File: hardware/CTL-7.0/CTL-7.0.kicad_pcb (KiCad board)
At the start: 2 copper layers, 18 parts, among them J2 Left, J3 Right, U1 STM32H750VBTx, U2 AMS1117-3.3, Y1 32.768K, Y2 25MHz

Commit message: modified:   Ferrite Transformer Calculation.xlsx 	modified:   archive/Peripheral Migration ESP32S3-STM32H7.md 	renamed:    archive/PR_ 0201_2026.docx -> archive/Purchase 20260201.docx 	new file:   archive/Purchase 20260720.docx 	new file:   archive/Purchase Plan/bom.csv 	new file:   archive/Purchase Plan/bom.xlsx 	new file:   archive/Purchase Recaps.xlsx 	modified:   archive/REM - Vsense.xlsx 	new file:   archive/datasheets/SPC7040.PDF 	new file:   archive/datasheets/rm0433-stm32h742-stm32h743-753-and-stm32h750-value-line-advanced-armbased-32bit-mcus-stmicroelectronics.pdf 	new file:   archive/refferences/MiniSTM32H7xx-master/.gitattributes 	new file:   archive/refferences/MiniSTM32H7xx-master/.gitignore 	new file:   archive/refferences/MiniSTM32H7xx-master/Datasheet/MCU/DM00287603_ZHV2.pdf 	new file:   "archive/refferences/MiniSTM32H7xx-master/Datasheet/MCU/ES0396_STM32H750xB\345\222\214STM32H753xI\345\215\225\347\211\207\346\234\272\347\232\204\345\261\200\351\231\220\346\200\247.pdf" 	new file:   "archive/refferences/MiniSTM32H7xx-master/Datasheet/MCU/PM0253_STM32F7\345\222\214 STM32H7\345\215\225\347\211\207\346\234\272\347\274\226\347\250\213\346\211\213\345\206\214.pdf" 	new file:   "archive/refferences/MiniSTM32H7xx-master/Datasheet/MCU/RM0433_STM32H7x3\345\222\214STM32H750\345\215\225\347\211\207\346\234\272\345\217\202\350\200\203\346\211\213\345\206\214.pdf" 	new file:   archive/refferences/MiniSTM32H7xx-master/Datasheet/MCU/STM32H743VI_Datasheet.pdf 	new file:   archive/refferences/MiniSTM32H7xx-master/Datasheet/MCU/STM32H750VB_Datasheet.pdf 	new file:   archive/refferences/MiniSTM32H7xx-master/Datasheet/MKESD0402MS05.PDF 	new file:   archive/refferences/MiniSTM32H7xx-master/Datasheet/ST7735S_V1.5_20150303.pdf 	new file:   archive/refferences/MiniSTM32H7xx-master/Datasheet/SY8088AAC.PDF 	new file:   archive/refferences/MiniSTM32H7xx-master/Datasheet/Sensor/OV2640-camera module.pdf 	new file:   archive/refferences/MiniSTM32H7xx-master/Datasheet/Sensor/OV26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
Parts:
- removed C1, C3: 10u, Capacitor_Tantalum_SMD:CP_EIA-3528-12_Kemet-T
- removed C2, C4: 100n, Capacitor_SMD:C_0805_2012Metric
- removed C5, C6: 10p, Capacitor_SMD:C_0805_2012Metric
- removed C7, C8: 20p, Capacitor_SMD:C_0805_2012Metric
- removed H1, H2, H3, H4: MountingHole_Pad, MountingHole:MountingHole_3mm_Pad
- removed J2: Left, Connector_PinHeader_2.54mm:PinHeader_2x22_P2.54mm_Vertical
- removed J3: Right, Connector_PinHeader_2.54mm:PinHeader_2x22_P2.54mm_Vertical
- removed U2: AMS1117-3.3, Package_TO_SOT_SMD:SOT-223-3_TabPin2
- removed Y1: 32.768K, Crystal:Crystal_SMD_3215-2Pin_3.2x1.5mm
- removed Y2: 25MHz, Crystal:Crystal_SMD_5032-2Pin_5.0x3.2mm
- U1: value STM32H750VBTx -> H750; footprint Package_QFP:LQFP-100_14x14mm_P0.5mm -> Core:STM32H750_v1
- moved U1 7.02 mm to (131.8, 98.2), turned to 0 degrees
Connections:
- U1 pad 100: +3.3V -> Net-(U1-+3.3V-Pad100)
- U1 pad 11: +3.3V -> Net-(U1-+3.3V-Pad100)
- U1 pad 12: Net-(U1-PH0) -> (no net)
- U1 pad 13: Net-(U1-PH1) -> (no net)
- U1 pad 21: unconnected-(U1-VDDA-Pad21) -> (no net)
- U1 pad 27: +3.3V -> Net-(U1-+3.3V-Pad100)
- U1 pad 50: +3.3V -> unconnected-(U1-+5V-Pad50)
- U1 pad 75: +3.3V -> Net-(U1-+3.3V-Pad100)
- U1 pad 8: Net-(U1-PC14) -> (no net)
- U1 pad 9: Net-(U1-PC15) -> (no net)
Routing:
- net Net-(U1-PH0): track 13.6 -> 0.00 mm
- net Net-(U1-PC14): track 12.4 -> 0.00 mm
- net Net-(U1-PC15): track 10.3 -> 0.00 mm
- net Net-(U1-PH1): track 9.88 -> 0.00 mm
- net unconnected-(U1-PC13-Pad7): track 7.93 -> 0.00 mm
- net unconnected-(U1-VBAT-Pad6): track 7.59 -> 0.00 mm
- net unconnected-(U1-PE6-Pad5): track 7.25 -> 0.00 mm
- net unconnected-(U1-PE5-Pad4): track 6.91 -> 0.00 mm
- net unconnected-(U1-PE4-Pad3): track 6.57 -> 0.00 mm
- net GND: track 6.35 -> 0.00 mm
- net unconnected-(U1-PE3-Pad2): track 6.24 -> 0.00 mm
- net unconnected-(U1-PE2-Pad1): track 5.90 -> 0.00 mm
- removed copper zone on F.Cu, net +3.3V
- removed copper zone on F.Cu, net +5V
- removed copper zone on B.Cu, net GND
- removed copper zone on F.Cu, net GND
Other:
- board outline added: 63.5 x 63.4 mm

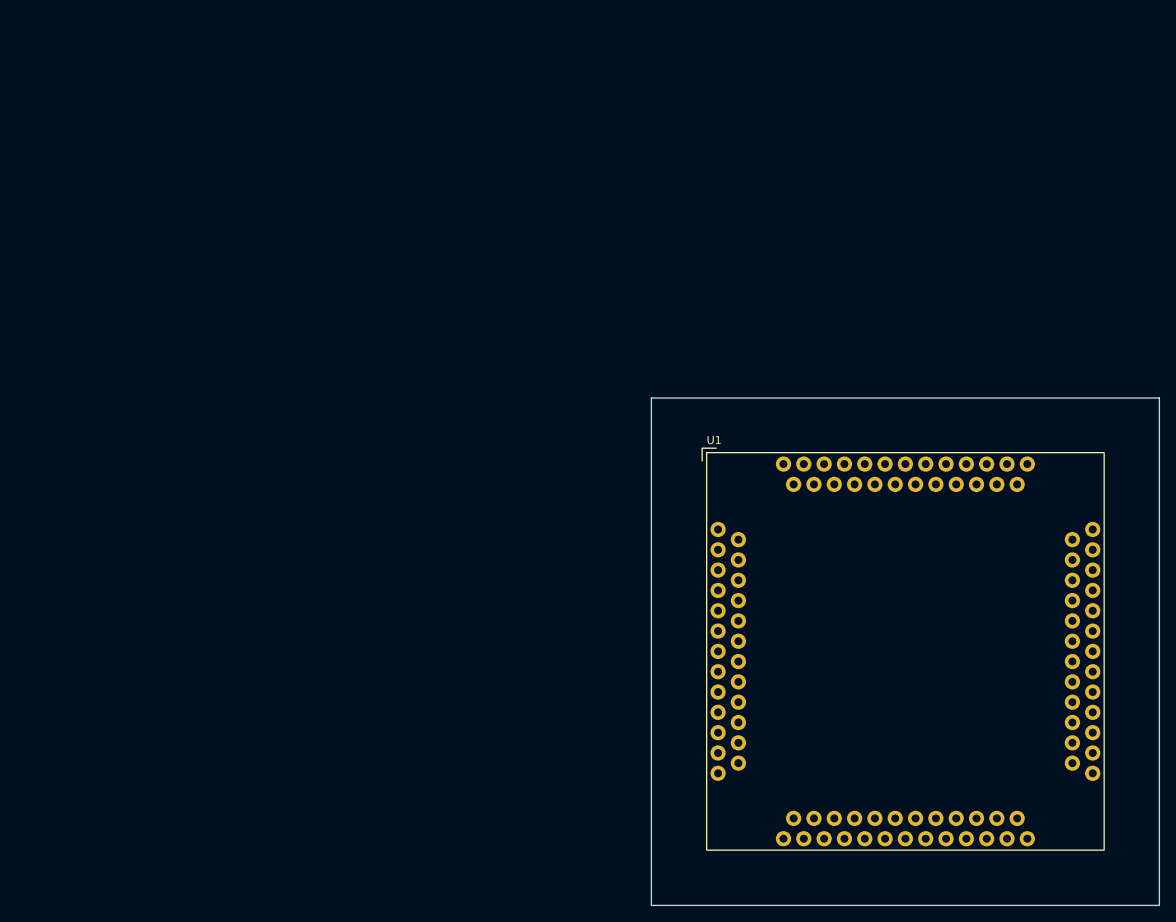
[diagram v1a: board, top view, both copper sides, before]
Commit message: modified:   archive/Peripheral Migration ESP32S3-STM32H7.md 	new file:   archive/refferences/STM32H750xB pin definition.xlsx 	new file:   archive/refferences/STM32H750xB_pin_definition-TIM_LPTIM_HRTIM.xlsx 	new file:   archive/refferences/pin alternatives.xlsx 	new file:   firmware/core-h750/.cproject 	new file:   firmware/core-h750/.mxproject 	new file:   firmware/core-h750/.osx.project 	new file:   firmware/core-h750/.project 	new file:   firmware/core-h750/.settings/language.settings.xml 	new file:   firmware/core-h750/.settings/org.eclipse.core.resources.prefs 	new file:   firmware/core-h750/.settings/stm32cubeide.project.prefs 	new file:   firmware/core-h750/Debug/Drivers/STM32H7xx_HAL_Driver/Src/stm32h7xx_hal.cyclo 	new file:   firmware/core-h750/Debug/Drivers/STM32H7xx_HAL_Driver/Src/stm32h7xx_hal.su 	new file:   firmware/core-h750/Debug/Drivers/STM32H7xx_HAL_Driver/Src/stm32h7xx_hal_cortex.cyclo 	new file:   firmware/core-h750/Debug/Drivers/STM32H7xx_HAL_Driver/Src/stm32h7xx_hal_cortex.su 	new file:   firmware/core-h750/Debug/Drivers/STM32H7xx_HAL_Driver/Src/stm32h7xx_hal_dma.cyclo 	new file:   firmware/core-h750/Debug/Drivers/STM32H7xx_HAL_Driver/Src/stm32h7xx_hal_dma.su 	new file:   firmware/core-h750/Debug/Drivers/STM32H7xx_HAL_Driver/Src/stm32h7xx_hal_dma_ex.cyclo 	new file:   firmware/core-h750/Debug/Drivers/STM32H7xx_HAL_Driver/Src/stm32h7xx_hal_dma_ex.su 	new file:   firmware/core-h750/Debug/Drivers/STM32H7xx_HAL_Driver/Src/stm32h7xx_hal_exti.cyclo 	new file:   firmware/core-h750/Debug/Drivers/STM32H7xx_HAL_Driver/Src/stm32h7xx_hal_exti.su 	new file:   firmware/core-h750/Debug/Drivers/STM32H7xx_HAL_Driver/Src/stm32h7xx_hal_flash.cyclo 	new file:   firmware/core-h750/Debug/Drivers/STM32H7xx_HAL_Driver/Src/stm32h7xx_hal_flash.su 	new file:   firmware/core-h750/Debug/Drivers/STM32H7xx_HAL_Driver/Src/stm32h7xx_hal_flash_ex.cyclo 	new file:   firmware/core-h750/Debug/Drivers/STM32H7xx_HAL_Driver/Src/stm32h7xx_hal_flash_ex.su 	new file:   firmware/core-h750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
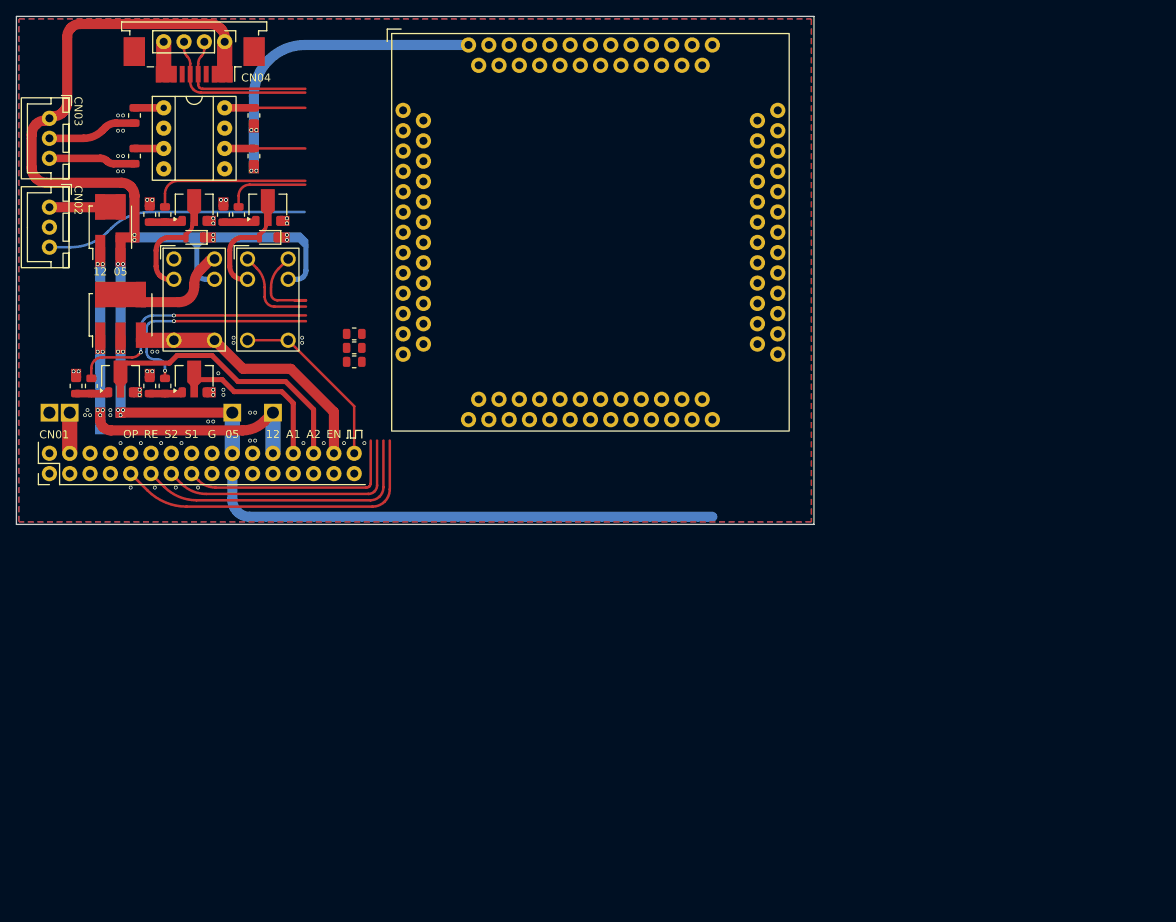
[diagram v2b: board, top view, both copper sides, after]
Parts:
- added CN01: Conn_02x16_Odd_Even, Connector_PinHeader_2.54mm:PinHeader_2x16_P2.54mm_Vertical, F.Cu at (24.8, 76.0)
- added CN02: Conn_01x03, Connector_JST:JST_XH_B3B-XH-A_1x03_P2.50mm_Vertical, F.Cu at (24.8, 45.2)
- added CN03: Conn_01x03, Connector_JST:JST_XH_B3B-XH-A_1x03_P2.50mm_Vertical, F.Cu at (24.8, 34.1)
- added CN04: ~, Connector_FFC-FPC:TE_1-84952-0_1x10-1MP_P1.0mm_Horizontal, F.Cu at (42.9, 24.3)
- added D1: 1N4148WS, Diode_SMD:D_SOD-323, F.Cu at (42.9, 46.5)
- added D2: 1N4148WS, Diode_SMD:D_SOD-323, F.Cu at (52.1, 46.5)
- added J1: Conn_02x02_Odd_Even, Connector_PinHeader_2.54mm:PinHeader_2x02_P2.54mm_Vertical_SMD, F.Cu at (32.4, 45.2)
- added J2: Conn_02x03_Odd_Even, Connector_PinHeader_2.54mm:PinHeader_2x03_P2.54mm_Vertical_SMD, F.Cu at (33.6, 56.2)
- added J3: Conn_01x04, Connector_PinHeader_2.54mm:PinHeader_1x04_P2.54mm_Vertical, F.Cu at (46.7, 22.1)
- added K1: G5V-1, Relay_THT:Relay_SPDT_Omron_G5V-1, F.Cu at (42.9, 49.2)
- added K2: G5V-1, Relay_THT:Relay_SPDT_Omron_G5V-1, F.Cu at (52.1, 49.2)
- added Q1: 2SK3605, Package_TO_SOT_SMD:SOT-89-3, F.Cu at (42.9, 42.4)
- added Q2: 2SK3605, Package_TO_SOT_SMD:SOT-89-3, F.Cu at (42.9, 63.9)
- added Q3: 2SK3605, Package_TO_SOT_SMD:SOT-89-3, F.Cu at (52.1, 42.4)
- added Q4: 2SK3605, Package_TO_SOT_SMD:SOT-89-3, F.Cu at (33.6, 63.9)
- added R10: 10k, Resistor_SMD:R_0805_2012Metric, F.Cu at (62.9, 60.3)
- added R11: 10k, Resistor_SMD:R_0805_2012Metric, F.Cu at (62.9, 58.6)
- added R19: 100, Resistor_SMD:R_0805_2012Metric, F.Cu at (39.2, 43.6)
- added R20: 10k, Resistor_SMD:R_0805_2012Metric, F.Cu at (37.3, 43.6)
- added R21: 100, Resistor_SMD:R_0805_2012Metric, F.Cu at (39.2, 65.1)
- added R22: 10k, Resistor_SMD:R_0805_2012Metric, F.Cu at (37.3, 65.1)
- added R23: 100, Resistor_SMD:R_0805_2012Metric, F.Cu at (48.4, 43.6)
- added R24: 10k, Resistor_SMD:R_0805_2012Metric, F.Cu at (46.5, 43.6)
- added R25: 100, Resistor_SMD:R_0805_2012Metric, F.Cu at (30.0, 65.1)
- added R26: 10k, Resistor_SMD:R_0805_2012Metric, F.Cu at (28.1, 65.1)
- added R5: 10k, Resistor_SMD:R_0805_2012Metric, F.Cu at (35.4, 31.3)
- added R6: 10k, Resistor_SMD:R_0805_2012Metric, F.Cu at (50.3, 31.3)
- added R7: 10k, Resistor_SMD:R_0805_2012Metric, F.Cu at (50.3, 36.3)
- added R8: 10k, Resistor_SMD:R_0805_2012Metric, F.Cu at (35.4, 36.3)
- added R9: 10k, Resistor_SMD:R_0805_2012Metric, F.Cu at (62.9, 62.1)
- added TP1: TestPoint, TestPoint:TestPoint_THTPad_2.2225x2.2225mm_Drill1.5mm, F.Cu at (27.3, 68.4)
- added TP2: TestPoint, TestPoint:TestPoint_THTPad_2.2225x2.2225mm_Drill1.5mm, F.Cu at (52.7, 68.4)
- added TP3: TestPoint, TestPoint:TestPoint_THTPad_2.2225x2.2225mm_Drill1.5mm, F.Cu at (47.6, 68.4)
- added TP4: TestPoint, TestPoint:TestPoint_THTPad_2.2225x2.2225mm_Drill1.5mm, F.Cu at (24.8, 68.4)
- added U6: PC827, Package_DIP:DIP-8_W7.62mm_Socket, F.Cu at (39.0, 30.3)
- moved U1 65.5 mm to (92.4, 45.9)
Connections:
- net Net-(U1-+3.3V-Pad100) renamed +3.3V
- U1 pad 50: unconnected-(U1-+5V-Pad50) -> +5V
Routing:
- net +5V: track 0.00 -> 166.1 mm, vias 0 -> 13
- net /OPTO: track 0.00 -> 46.1 mm
- net /REM: track 0.00 -> 42.0 mm
- net /MSD2: track 0.00 -> 37.8 mm
- net /RLY2-A: track 0.00 -> 37.8 mm
- net /PWM-EN: track 0.00 -> 37.8 mm
- net +3.3V: track 0.00 -> 37.2 mm, vias 0 -> 4
- net /MSD1: track 0.00 -> 33.7 mm
- net +12V: track 0.00 -> 33.6 mm, vias 0 -> 7
- net /BUZZ: track 0.00 -> 33.1 mm
- net /CTL-RLY2: track 0.00 -> 33.0 mm, vias 0 -> 2
- net /CTL-RLY1: track 0.00 -> 28.1 mm, vias 0 -> 2
- net /PWM: track 0.00 -> 27.7 mm
- net /RLY1-A: track 0.00 -> 24.9 mm
- net /LCD_RX: track 0.00 -> 20.3 mm
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- added copper zone on B.Cu, net GND
- added copper zone on F.Cu, net GND
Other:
- board size 63.5 x 63.4 mm -> 99.7 x 63.5 mm
- board text added: "05"
- board text added: "12"
- board text added: "A1"
- board text added: "A2"
- board text added: "EN"
- board text added: "G"
- board text added: "OP"
- board text added: "RE"
- board text added: "S1"
- board text added: "S2"
